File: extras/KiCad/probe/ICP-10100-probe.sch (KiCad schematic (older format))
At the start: 13 parts, among them J1 Conn_01x04, Q1 UM6K34NTCN, U1 ICP-10100, U2 AP7313R

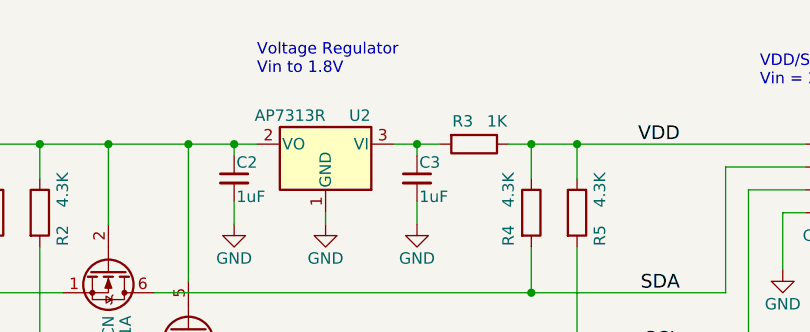
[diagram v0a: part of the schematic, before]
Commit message: add note about reversed footprint of LDO
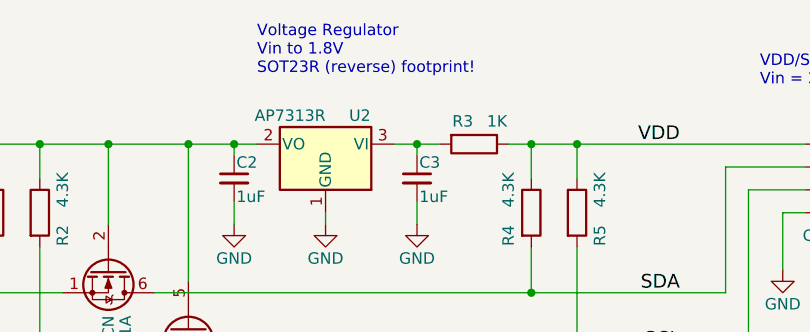
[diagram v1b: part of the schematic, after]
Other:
- note added: "Voltage Regulator\nVin to 1.8V\nSOT23R (reverse) footprint!"
- note removed: "Voltage Regulator\nVin to 1.8V"
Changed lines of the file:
@@
 VDD/SDA/SCL\nVin = 2.8V to 5V
 Text Notes 7000 2500 0    50   ~ 0
-Voltage Regulator\nVin to 1.8V
+Voltage Regulator\nVin to 1.8V\nSOT23R (reverse) footprint!
 Text Notes 6300 4550 0    50   ~ 0
 Level-Shifter\nVin to 1.8V

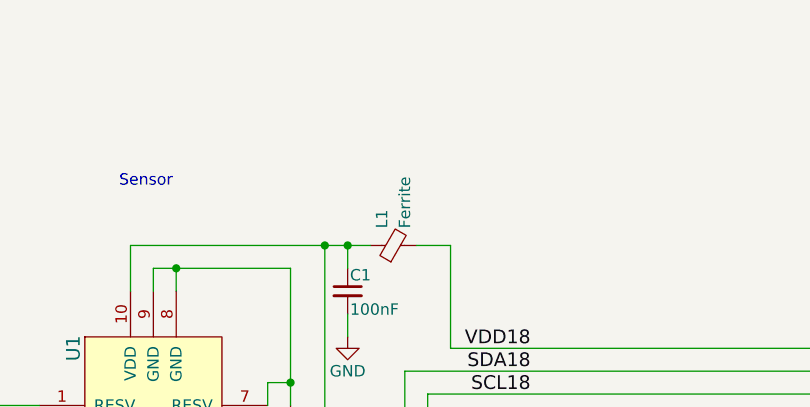
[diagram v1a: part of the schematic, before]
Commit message: add part number for L1, clean-up metadata
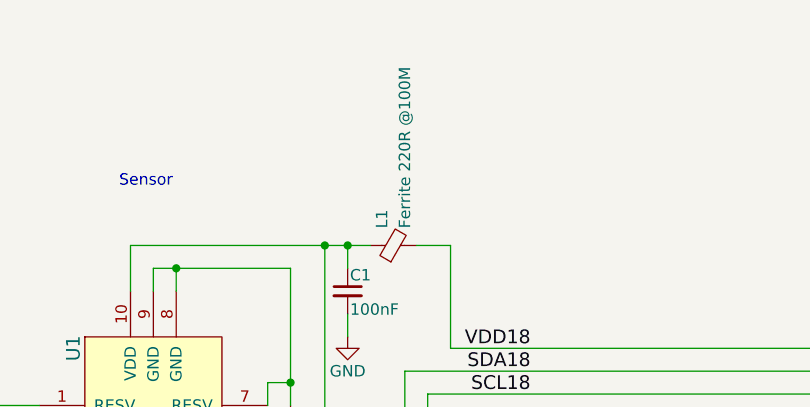
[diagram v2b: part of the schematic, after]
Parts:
- C1, C2, J1, R1, R2, R3, R4, R5: Dist Link Value -> (none); Dist PN Value -> (none)
- L1: value Ferrite -> Ferrite 220R @100M; Dist Link Value -> (none); Dist PN Value -> (none); Mpn (none) -> BLM15PX221SN1D
- Q1: Dist Link Value -> (none); Dist PN Value -> (none); MFG Name ROHM -> (none); MFG Part Num UM6K34NTCN -> (none); Mpn (none) -> UM6K34NTCN
- Q1: Mpn (none) -> UM6K34NTCN
- U1: Dist Link Value -> (none); Dist PN Value -> (none); MFG Name TDK -> (none); MFG Part Num ICP-10100 -> (none); Mpn (none) -> ICP-10100
- U2: footprint Package_TO_SOT_SMD:SOT-23 -> Package_TO_SOT_SMD:SOT-223-3_TabPin2; Dist Link Value -> (none); Dist PN Value -> (none); MFG Name Diodes Inc -> (none); MFG Part Num AP7313-18SRG-7 -> (none); Mpn (none) -> AP7313-18SRG-7
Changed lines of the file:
@@
 F 2 "footprints:ICP-10100" H 2500 3500 60  0001 C CNN
 F 3 "" H 2500 3500 60  0001 C CNN
-F 4 "TDK" H 2500 3500 60  0001 C CNN "MFG Name"
-F 5 "ICP-10100" H 2500 3500 60  0001 C CNN "MFG Part Num"
-F 6 "Value" H 2500 3500 60  0001 C CNN "Dist PN"
-F 7 "Value" H 2500 3500 60  0001 C CNN "Dist Link"
+F 4 "ICP-10100" H 2500 3500 50  0001 C CNN "Mpn"
 	1    2500 3500
 	1    0    0    -1
@@
 F 2 "Capacitor_SMD:C_0402_1005Metric" H 3350 2900 50  0001 C CNN
 F 3 "" H 3350 2900 50  0001 C CNN
-F 4 "Value" H 3350 2900 60  0001 C CNN "Dist PN"
-F 5 "Value" H 3350 2900 60  0001 C CNN "Dist Link"
 	1    3350 2900
 	1    0    0    -1
@@
 F 2 "Package_TO_SOT_SMD:SOT-363_SC-70-6" H 6900 3525 50  0001 L CIN
 F 3 "" H 6700 3600 50  0001 L CNN
+F 4 "UM6K34NTCN" H 6700 3600 50  0001 C CNN "Mpn"
 	2    6700 3600
 	0    1    1    0
@@
 F 2 "Resistor_SMD:R_0603_1608Metric" V 5980 3100 50  0001 C CNN
 F 3 "" H 6050 3100 50  0001 C CNN
-F 4 "Value" H 6050 3100 60  0001 C CNN "Dist PN"
-F 5 "Value" H 6050 3100 60  0001 C CNN "Dist Link"
 	1    6050 3100
 	1    0    0    -1
@@
 F 2 "Resistor_SMD:R_0603_1608Metric" V 8330 3100 50  0001 C CNN
 F 3 "" H 8400 3100 50  0001 C CNN
-F 4 "Value" H 8400 3100 60  0001 C CNN "Dist PN"
-F 5 "Value" H 8400 3100 60  0001 C CNN "Dist Link"
 	1    8400 3100
 	1    0    0    -1
@@
 F 2 "Resistor_SMD:R_0603_1608Metric" V 8130 3100 50  0001 C CNN
 F 3 "" H 8200 3100 50  0001 C CNN
-F 4 "Value" H 8200 3100 60  0001 C CNN "Dist PN"
-F 5 "Value" H 8200 3100 60  0001 C CNN "Dist Link"
 	1    8200 3100
 	1    0    0    -1
@@
 F 0 "U2" H 7150 2925 50  0000 C CNN
 F 1 "AP7313R" H 7300 2925 50  0000 L CNN
-F 2 "Package_TO_SOT_SMD:SOT-23" H 7300 3000 50  0001 C CNN
+F 2 "Package_TO_SOT_SMD:SOT-223-3_TabPin2" H 7300 3000 50  0001 C CNN
 F 3 "" H 7400 2550 50  0001 C CNN
-F 4 "Diodes Inc" H 7300 2800 60  0001 C CNN "MFG Name"
-F 5 "AP7313-18SRG-7" H 7300 2800 60  0001 C CNN "MFG Part Num"
-F 6 "Value" H 7300 2800 60  0001 C CNN "Dist PN"
-F 7 "Value" H 7300 2800 60  0001 C CNN "Dist Link"
+F 4 "AP7313-18SRG-7" H 7300 2800 50  0001 C CNN "Mpn"
 	1    7300 2800
 	-1   0    0    -1
@@
 F 2 "Capacitor_SMD:C_0402_1005Metric" H 6900 2950 50  0001 C CNN
 F 3 "" H 6900 2950 50  0001 C CNN
-F 4 "Value" H 6900 2950 60  0001 C CNN "Dist PN"
-F 5 "Value" H 6900 2950 60  0001 C CNN "Dist Link"
 	1    6900 2950
 	1    0    0    -1
@@
 F 2 "Resistor_SMD:R_0603_1608Metric" V 7880 2800 50  0001 C CNN
 F 3 "" H 7950 2800 50  0001 C CNN
-F 4 "Value" H 7950 2800 60  0001 C CNN "Dist PN"
-F 5 "Value" H 7950 2800 60  0001 C CNN "Dist Link"
 	1    7950 2800
 	0    1    1    0
@@
 F 2 "Connector_PinHeader_2.54mm:PinHeader_1x04_P2.54mm_Vertical" H 9600 2900 50  0001 C CNN
 F 3 "" H 9600 2900 50  0001 C CNN
-F 4 "Value" H 9600 2900 60  0001 C CNN "Dist PN"
-F 5 "Value" H 9600 2900 60  0001 C CNN "Dist Link"
 	1    9600 2900
 	1    0    0    -1
@@
 P 3550 2700
 F 0 "L1" H 3625 2750 50  0000 L CNN
-F 1 "Ferrite" H 3625 2650 50  0000 L CNN
+F 1 "Ferrite 220R @100M" H 3625 2650 50  0000 L CNN
 F 2 "Capacitor_SMD:C_0402_1005Metric" V 3480 2700 50  0001 C CNN
 F 3 "" H 3550 2700 50  0001 C CNN
-F 4 "Value" H 3550 2700 60  0001 C CNN "Dist PN"
-F 5 "Value" H 3550 2700 60  0001 C CNN "Dist Link"
+F 4 "BLM15PX221SN1D" H 3550 2700 50  0001 C CNN "Mpn"
 	1    3550 2700
 	0    -1   -1   0
@@
 F 2 "Package_TO_SOT_SMD:SOT-363_SC-70-6" H 6550 3275 50  0001 L CIN
 F 3 "" H 6350 3350 50  0001 L CNN
-F 4 "ROHM" H 6350 3350 60  0001 C CNN "MFG Name"
-F 5 "UM6K34NTCN" H 6350 3350 60  0001 C CNN "MFG Part Num"
-F 6 "Value" H 6350 3350 60  0001 C CNN "Dist PN"
-F 7 "Value" H 6350 3350 60  0001 C CNN "Dist Link"
+F 4 "UM6K34NTCN" H 6350 3350 50  0001 C CNN "Mpn"
 	1    6350 3350
 	0    1    1    0
@@
 F 2 "Resistor_SMD:R_0603_1608Metric" V 5780 3100 50  0001 C CNN
 F 3 "" H 5850 3100 50  0001 C CNN
-F 4 "Value" H 5850 3100 60  0001 C CNN "Dist PN"
-F 5 "Value" H 5850 3100 60  0001 C CNN "Dist Link"
 	1    5850 3100
 	1    0    0    -1
